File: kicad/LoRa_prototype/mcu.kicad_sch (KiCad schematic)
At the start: 54 parts, among them J14 SPI_FLASH, J16 I2C1, J17 UART1, J18 MCO, SW1 NRST, U10 STM32WL54CCUx, U8 W25Q16JVSS, X1 32768Hz, X2 NT2016SF

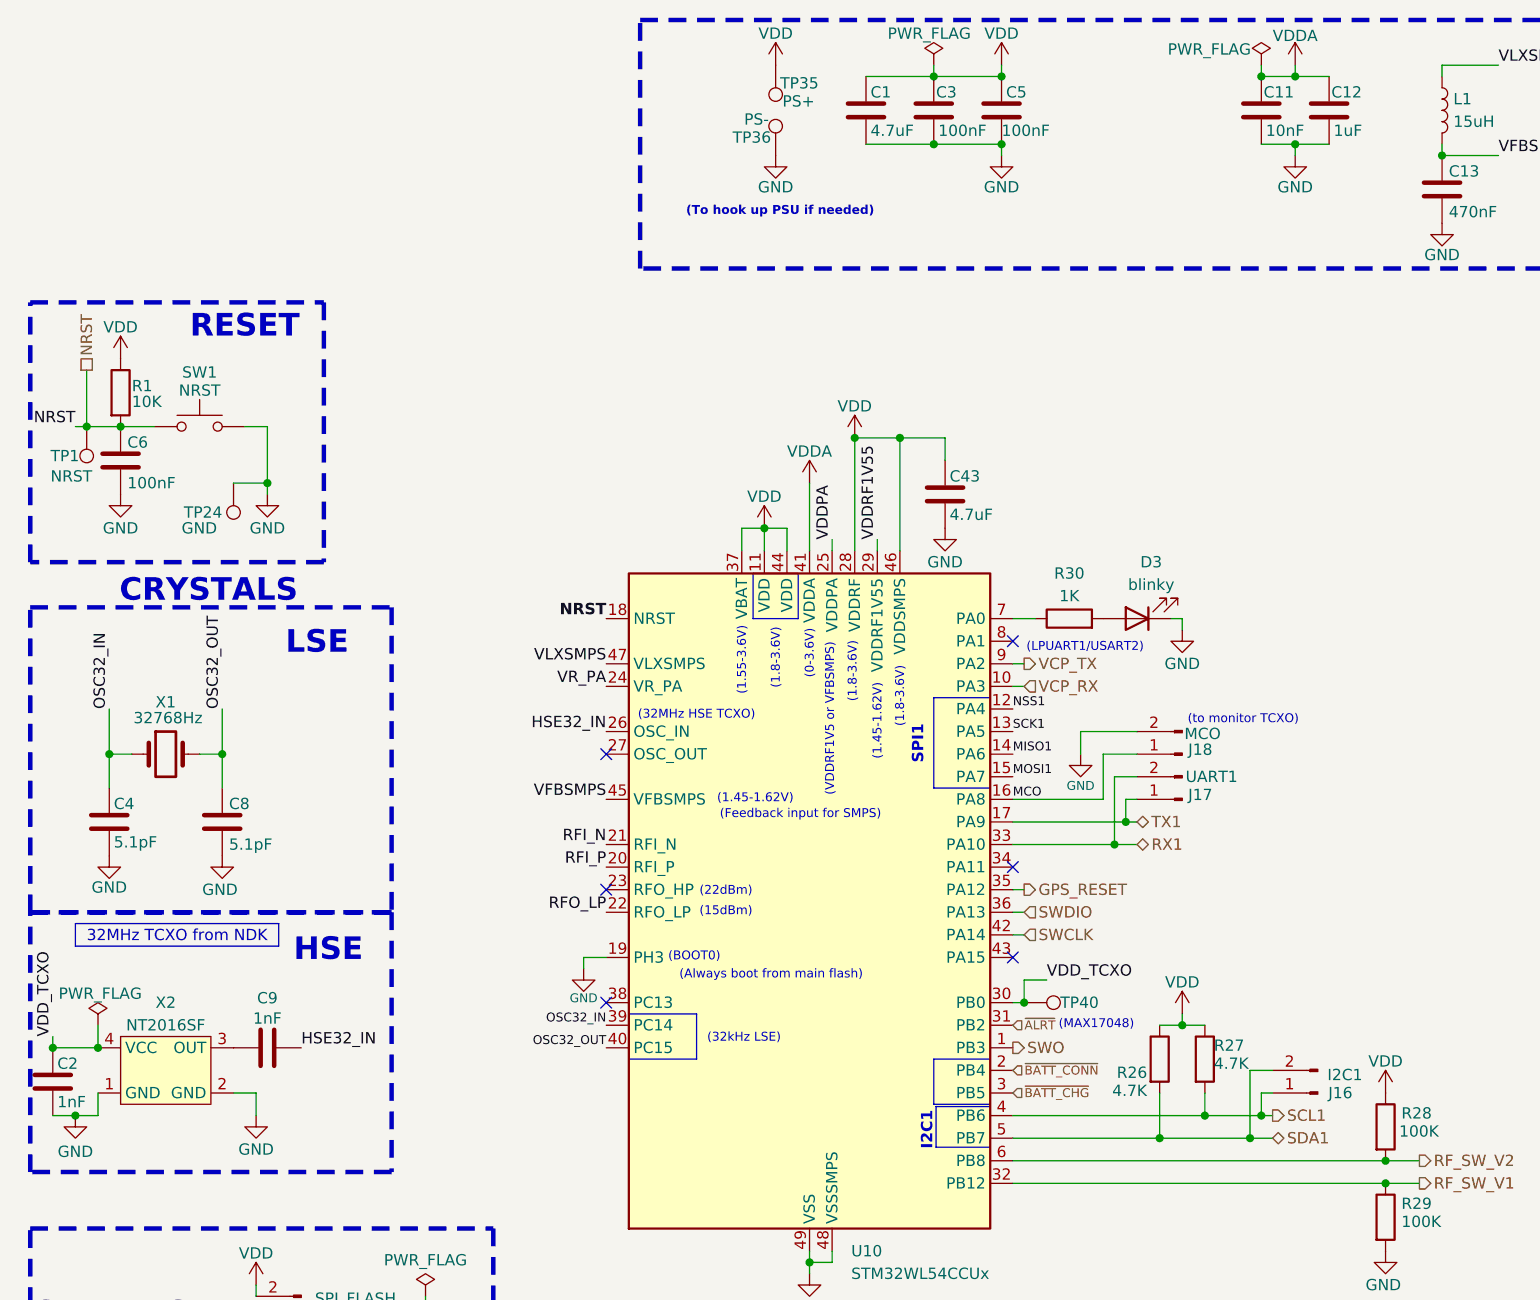
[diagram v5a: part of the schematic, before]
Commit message: Added ESD protection to I2C and UART headers
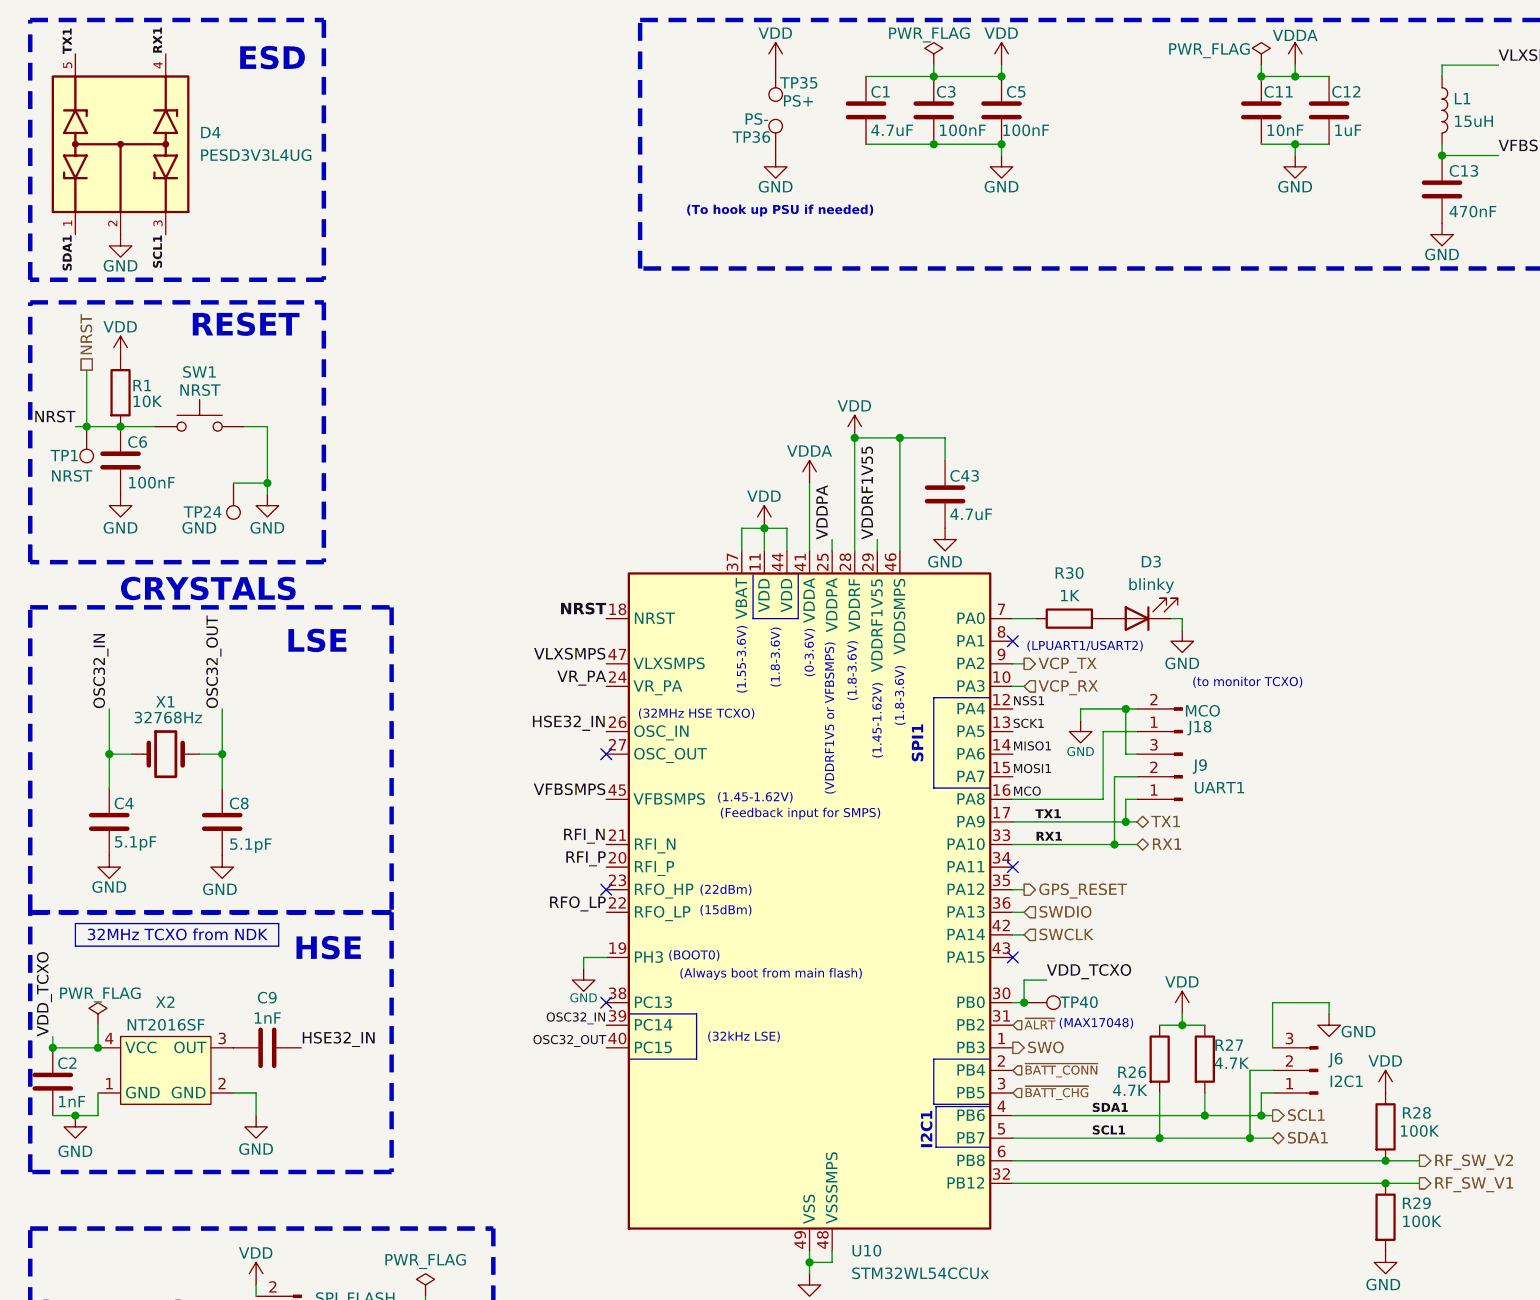
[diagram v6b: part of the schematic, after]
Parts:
- removed J16: I2C1, Connector_PinHeader_2.54mm:PinHeader_1x02_P2.54mm_Vertical, symbol Connector:Conn_01x02_Pin
- removed J17: UART1, Connector_PinHeader_2.54mm:PinHeader_1x02_P2.54mm_Vertical, symbol Connector:Conn_01x02_Pin
- added D4: PESD3V3L4UG, PESD3V3L4UG:DIO_PESD3V3L4UG, symbol PESD3V3L4UG:PESD3V3L4UG
- added J6: I2C1, Connector_PinHeader_2.54mm:PinHeader_1x03_P2.54mm_Vertical, symbol Connector:Conn_01x03_Pin
- added J9: UART1, symbol Connector:Conn_01x03_Pin
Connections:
- net SDA1 is gone; now on net SCL1: R26.2, U10.5 (PB7)
- net GND: now also D4.2, J6.3 (Pin_3), J9.3 (Pin_3)
- net RX1: now also D4.4, J9.2 (Pin_2)
- net SCL1: now also D4.1, D4.3, J6.1 (Pin_1), J6.2 (Pin_2)
- net TX1: now also D4.5, J9.1 (Pin_1)
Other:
- note added: "ESD"
- moved on the sheet: J18

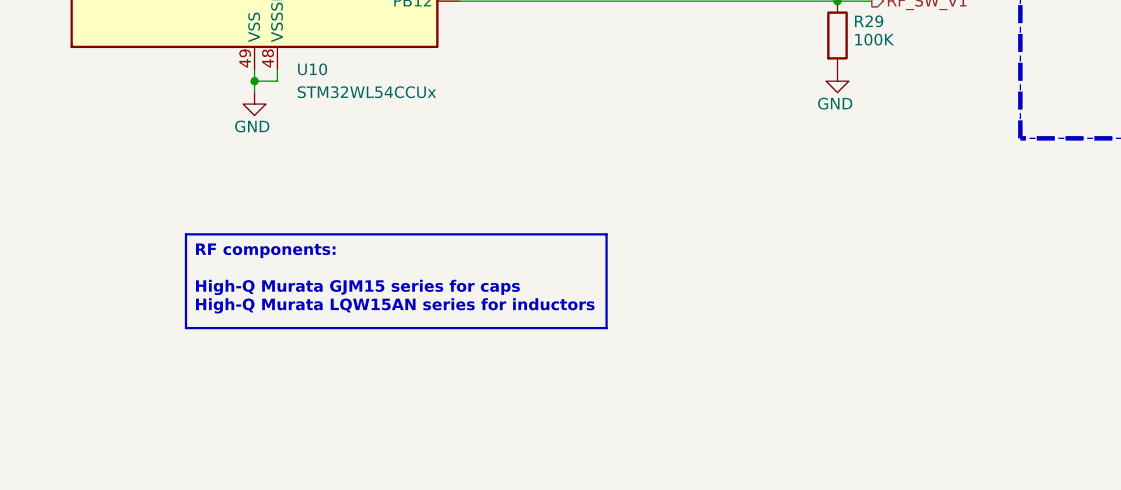
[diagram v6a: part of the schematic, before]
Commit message: Assigned most footprints
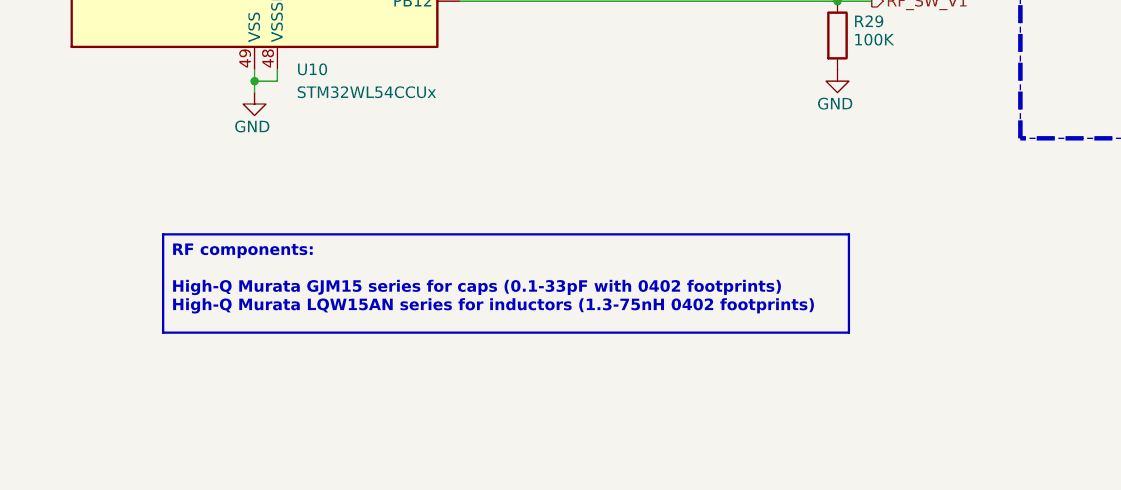
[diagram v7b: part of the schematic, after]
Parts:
- C14, C20, C21, C22, C24, C25, C26, C4, C8: footprint Capacitor_SMD:C_0805_2012Metric -> Capacitor_SMD:C_0402_1005Metric
- L1, L2, L3, L4, L5, L6: footprint (none) -> Inductor_SMD:L_0402_1005Metric
- TP1, TP24: footprint (none) -> TestPoint:TestPoint_Pad_2.0x2.0mm
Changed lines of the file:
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@@
 		)
 	)
-	(text_box "RF components:\n\nHigh-Q Murata GJM15 series for caps\nHigh-Q Murata LQW15AN series for inductors\n\n"
+	(text_box "RF components:\n\nHigh-Q Murata GJM15 series for caps (0.1-33pF with 0402 footprints)\nHigh-Q Murata LQW15AN series for inductors (1.3-75nH 0402 footprints)\n\n"
 		(exclude_from_sim no)
-		(at 93.98 169.418 0)
-		(size 46.736 10.4163)
+		(at 91.44 169.418 0)
+		(size 76.2 10.9219)
 		(margins 0.9525 0.9525 0.9525 0.9525)
 		(stroke
@@
 			)
 		)
-		(property "Footprint" ""
+		(property "Footprint" "TestPoint:TestPoint_Pad_2.0x2.0mm"
 			(at 31.75 64.77 0)
 			(hide yes)
@@
 			)
 		)
-		(property "Footprint" ""
+		(property "Footprint" "Inductor_SMD:L_0402_1005Metric"
 			(at 247.65 93.98 0)
 			(hide yes)
@@
 			)
 		)
-		(property "Footprint" "Capacitor_SMD:C_0805_2012Metric"
+		(property "Footprint" "Capacitor_SMD:C_0402_1005Metric"
 			(at 36.5252 106.68 0)
 			(hide yes)
@@
 			)
 		)
-		(property "Footprint" "Capacitor_SMD:C_0805_2012Metric"
+		(property "Footprint" "Capacitor_SMD:C_0402_1005Metric"
 			(at 23.8252 106.68 0)
 			(hide yes)
@@
 			)
 		)
-		(property "Footprint" ""
+		(property "Footprint" "Inductor_SMD:L_0402_1005Metric"
 			(at 172.72 22.86 0)
 			(hide yes)
@@
 			)
 		)
-		(property "Footprint" "Capacitor_SMD:C_0805_2012Metric"
+		(property "Footprint" "Capacitor_SMD:C_0402_1005Metric"
 			(at 216.8652 31.75 0)
 			(hide yes)
@@
 			)
 		)
-		(property "Footprint" "Capacitor_SMD:C_0805_2012Metric"
+		(property "Footprint" "Capacitor_SMD:C_0402_1005Metric"
 			(at 226.06 132.3848 0)
 			(hide yes)
@@
 			)
 		)
-		(property "Footprint" "Capacitor_SMD:C_0805_2012Metric"
+		(property "Footprint" "Capacitor_SMD:C_0402_1005Metric"
 			(at 227.0252 149.86 0)
 			(hide yes)
@@
 			)
 		)
-		(property "Footprint" "Capacitor_SMD:C_0805_2012Metric"
+		(property "Footprint" "Capacitor_SMD:C_0402_1005Metric"
 			(at 251.1552 149.86 0)
 			(hide yes)
@@
 			)
 		)
-		(property "Footprint" "Capacitor_SMD:C_0805_2012Metric"
+		(property "Footprint" "Capacitor_SMD:C_0402_1005Metric"
 			(at 248.6152 105.41 0)
 			(hide yes)
@@
 			)
 		)
-		(property "Footprint" ""
+		(property "Footprint" "Inductor_SMD:L_0402_1005Metric"
 			(at 215.9 124.46 0)
 			(hide yes)
@@
 			)
 		)
-		(property "Footprint" "Capacitor_SMD:C_0805_2012Metric"
+		(property "Footprint" "Capacitor_SMD:C_0402_1005Metric"
 			(at 257.81 89.2048 0)
 			(hide yes)
@@
 			)
 		)
-		(property "Footprint" ""
+		(property "Footprint" "Inductor_SMD:L_0402_1005Metric"
 			(at 242.57 139.7 0)
 			(hide yes)
@@
 			)
 		)
-		(property "Footprint" ""
+		(property "Footprint" "Inductor_SMD:L_0402_1005Metric"
 			(at 212.09 139.7 0)
 			(hide yes)
@@
 			)
 		)
-		(property "Footprint" ""
+		(property "Footprint" "TestPoint:TestPoint_Pad_2.0x2.0mm"
 			(at 15.24 58.42 0)
 			(hide yes)
@@
 			)
 		)
-		(property "Footprint" "Capacitor_SMD:C_0805_2012Metric"
+		(property "Footprint" "Capacitor_SMD:C_0402_1005Metric"
 			(at 219.4052 149.86 0)
 			(hide yes)
@@
 			)
 		)
-		(property "Footprint" ""
+		(property "Footprint" "Inductor_SMD:L_0402_1005Metric"
 			(at 222.25 139.7 0)
 			(hide yes)

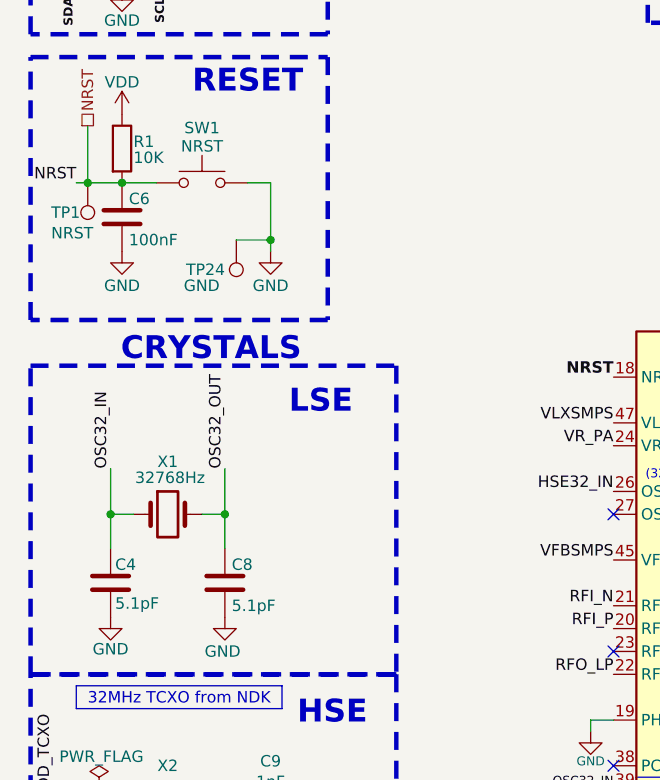
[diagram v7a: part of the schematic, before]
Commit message: Assigned almost all footprints
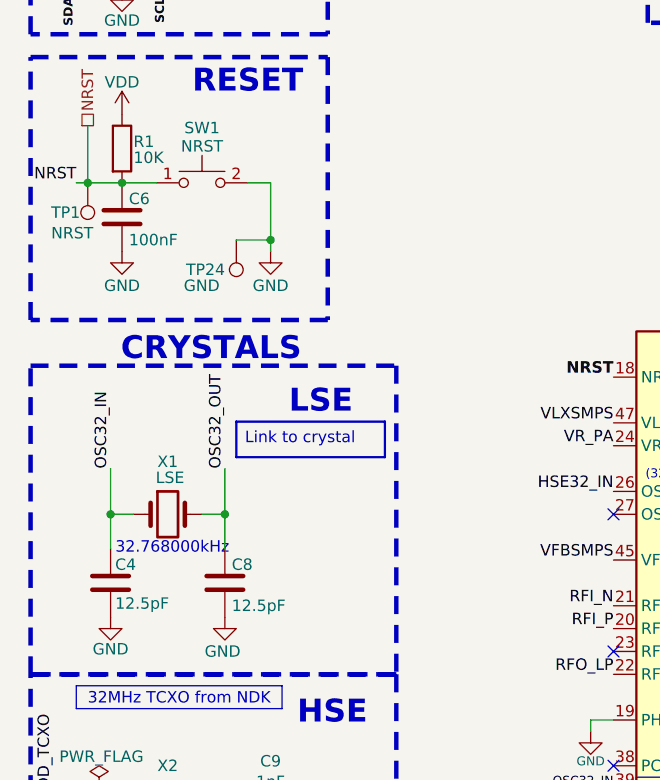
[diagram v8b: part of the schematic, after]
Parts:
- C4, C8: value 5.1pF -> 12.5pF
- J9: footprint (none) -> Connector_PinHeader_2.54mm:PinHeader_1x03_P2.54mm_Vertical
- SW1: footprint (none) -> footprints:TS-1088-AR02016
- X1: value 32768Hz -> LSE; footprint (none) -> Crystal:Crystal_SMD_3215-2Pin_3.2x1.5mm
- X2: footprint (none) -> footprints:NT2016SF TCXO
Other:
- note added: "32.768000kHz"
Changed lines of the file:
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@@
 		)
 	)
+	(text "32.768000kHz"
+		(exclude_from_sim no)
+		(at 29.718 99.06 0)
+		(effects
+			(font
+				(size 1.27 1.27)
+				(thickness 0.1588)
+			)
+		)
+	)
 	(text "(Always boot from main flash)"
 		(exclude_from_sim no)
@@
 		)
 	)
+	(text_box "Link to crystal"
+		(exclude_from_sim no)
+		(at 36.83 84.9517 0)
+		(size 16.51 3.9483)
+		(margins 0.9525 0.9525 0.9525 0.9525)
+		(stroke
+			(width 0.25)
+			(type solid)
+		)
+		(fill
+			(type color)
+			(color 247 255 80 1)
+		)
+		(effects
+			(font
+				(size 1.27 1.27)
+			)
+			(justify left top)
+			(href "https://jlcpcb.com/partdetail/SeikoEpson-Q13FC13500004/C32346")
+		)
+	)
 	(junction
 		(at 20.32 58.42)
@@
 			)
 		)
-		(property "Value" "5.1pF"
+		(property "Value" "12.5pF"
 			(at 36.322 105.41 0)
 			(show_name no)
@@
 			)
 		)
-		(property "Value" "5.1pF"
+		(property "Value" "12.5pF"
 			(at 23.368 105.156 0)
 			(show_name no)
@@
 			)
 		)
-		(property "Footprint" ""
+		(property "Footprint" "footprints:NT2016SF TCXO"
 			(at 29.21 130.81 0)
 			(hide yes)
@@
 			)
 		)
-		(property "Value" "32768Hz"
+		(property "Value" "LSE"
 			(at 29.464 91.186 0)
 			(show_name no)
@@
 			)
 		)
-		(property "Footprint" ""
+		(property "Footprint" "Crystal:Crystal_SMD_3215-2Pin_3.2x1.5mm"
 			(at 29.21 95.25 0)
 			(hide yes)
@@
 			)
 		)
-		(property "Footprint" ""
+		(property "Footprint" "Connector_PinHeader_2.54mm:PinHeader_1x03_P2.54mm_Vertical"
 			(at 143.51 97.79 0)
 			(hide yes)
@@
 			)
 		)
-		(property "Footprint" ""
+		(property "Footprint" "footprints:TS-1088-AR02016"
 			(at 33.02 53.34 0)
 			(hide yes)
@@
 		)
 	)
+	(group "Crystals"
+		(members "0131010e-98cc-4511-bc0d-da0821f78244" "0ef9bd5a-c4a4-4c0f-bbc5-0c07e9539615"
+			"1c9b325f-f363-4d43-b3c1-4fdfe486076c" "1ca60008-4da7-498b-aaa0-9d833e48a596"
+			"24139092-2a8e-4ab9-9936-116e0282de1c" "265b02d9-6a0d-4f13-b8f8-cc6d24663a78"
+			"2fa8d7e8-c419-4d84-88ac-592225dd1e38" "3d5edb10-198e-4fc4-b183-cb62556fddab"
+			"456f71d9-53ae-423e-93b4-e91a0128f17b" "509a1b49-96e9-4c18-bc11-75d18778e8fb"
+			"56e0e92b-6608-4598-8e7e-4001b705daee" "5e01ecd7-3b4a-4071-bb2c-c6c4f9b3d0fa"
+			"5f91d072-0735-413a-8cf8-4a735734da00" "5ff36ed1-f2dd-4430-8767-1af45fbd1308"
+			"6131293a-8fce-4cc9-b89b-8d7c416ecb18" "66fa982f-530c-43b3-a9ce-1f48db05f8d7"
+			"701c7268-9f04-4945-99b3-cbf8d4b63182" "76f07008-22d8-4496-8804-9008ee6c769e"
+			"897af834-9615-4c5a-82f2-47e6c4795b25" "8a5685ef-b085-4a06-b8aa-d69b1dc9044c"
+			"8e6f1584-c634-4891-8627-9f080d4bb6a8" "a243fc16-e60f-4e84-bd24-a123b049121d"
+			"a3182571-d53f-4851-866b-1001ee527e47" "b239c4a0-c314-4429-ad64-e2093f4a6479"
+			"b572338d-d7e6-4be2-918d-5daf0286e604" "bc609901-e3b2-4125-9b6c-29d793086d56"
+			"be060f7d-4bbe-4f7b-b7fd-078a4809f604" "c3802325-eaef-4699-9c16-c4e7df9fb6a2"
+			"cbe89259-d560-4aa9-9e10-341d9fb401e9" "ccf29687-3704-4176-a5cf-5e555e5b6c5c"
+			"d2d8415e-33b7-4946-9a0b-e68025cf207c" "d84d963b-c5ec-48db-b242-4ee6881accfa"
+			"e0de5d6f-8c78-4710-90ec-a8162c3f8272" "e0effaa2-fd82-492a-849c-1e8c1032e8cd"
+			"e1483134-8060-4edd-9c27-c2b11b432545" "e6c9a3da-3457-4937-86b4-4c9e760a02fa"
+			"ecf1838b-fdf1-4b15-b61d-df3f309df102" "f34baa0a-7b7d-4bf8-a3ca-3d2ec8693c74"
+			"f5282f99-961a-4e28-9c73-eefa68f63610" "f55a2e63-dc3b-4bb3-9995-00b8e2bcfde1"
+			"f8dcf6eb-8a98-4a92-b8eb-58113ac46de4" "fba21304-e36a-4a4e-b3fb-8888c43f7868"
+			"fc686b08-daae-4007-b1a2-6f28f4b95fcc"
+		)
+	)
